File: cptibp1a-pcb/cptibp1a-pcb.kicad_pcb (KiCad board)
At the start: 2 copper layers, 50.5 x 42 mm, 28 parts, among them J1 10118194-0001LF, J2 PAD+, J3 PAD-, Q1 2N7002, Q2 AO3413, U1 NCP360SNT, U2 APX809S-31SA, U3 BQ21040, U4 APX810S-44SA, U5 NCP380HSN05

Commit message: cleanup
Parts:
- added REF**: ENCLOSURE, george:ENCLOSURE, F.Cu at (0.00, 0.00)
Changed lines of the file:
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@@
     )
   )
+  (footprint "george:ENCLOSURE" (layer "F.Cu")
+    (at 0 0)
+    (attr board_only allow_missing_courtyard)
+    (fp_text reference "REF**" (at 0 -0.5 unlocked) (layer "F.SilkS") hide
+        (effects (font (size 1 1) (thickness 0.15)))
+    )
+    (fp_text value "ENCLOSURE" (at 0 -4 unlocked) (layer "F.Fab")
+        (effects (font (size 1 1) (thickness 0.15)))
+    )
+    (fp_text user "${REFERENCE}" (at 0 4 unlocked) (layer "F.Fab")
+        (effects (font (size 1 1) (thickness 0.15)))
+    )
+    (fp_line (start -3 0) (end 3 0)
+      (stroke (width 0.12) (type default)) (layer "Dwgs.User"))
+    (fp_line (start 0 -3) (end 0 3)
+      (stroke (width 0.12) (type default)) (layer "Dwgs.User"))
+    (fp_circle (center 0 0) (end 0 -2)
+      (stroke (width 0.12) (type default)) (fill none) (layer "Dwgs.User"))
+  )
   (footprint "Capacitor_SMD:C_0805_2012Metric" (layer "F.Cu")
     (at 0.5 35.5 -90)
@@
   (gr_rect (start -12.6 27) (end -10 28.6)
     (stroke (width 0.15) (type default)) (fill none) (layer "F.SilkS"))
-  (gr_rect (start -0.2 25.5) (end 1.5 22.9)
+  (gr_rect (start -0.2 22.9) (end 1.5 25.5)
     (stroke (width 0.15) (type default)) (fill none) (layer "F.SilkS"))
   (gr_line (start -24.2 21.2) (end -23.8 20.8)
@@
   (gr_rect (start -9.7 18.6) (end -6.8 21.6)
     (stroke (width 0.15) (type default)) (fill none) (layer "F.SilkS"))
-  (gr_rect (start 5.65 27.65) (end 2.35 24.75)
+  (gr_rect (start 2.35 24.75) (end 5.65 27.65)
     (stroke (width 0.15) (type default)) (fill none) (layer "F.SilkS"))
-  (gr_rect (start 0.85 22.6) (end 6.45 19.4)
+  (gr_rect (start 0.85 19.4) (end 6.45 22.6)
     (stroke (width 0.15) (type default)) (fill none) (layer "F.SilkS"))
   (gr_rect (start -24.3 18.6) (end -21.7 20.3)

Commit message: rev1
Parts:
- added C3: 4u7, Capacitor_SMD:C_0805_2012Metric, F.Cu at (1.50, 39.1)
- added R6: 10k, Resistor_SMD:R_0805_2012Metric, F.Cu at (5.80, 35.5)
- added U6: NCP380HSN05, george:SOT-23-5_TI_DBV5, F.Cu at (4.70, 39.0)
- U5: value NCP380HSN05 -> MAX40203AUK
- moved U5 1.95 mm to (2.70, 35.5), turned to 0 degrees
- moved C2 1.76 mm to (-9.30, 39.1)
- moved U4 1.20 mm to (-5.59, 39.0)
- moved Q2 1.20 mm to (-1.50, 39.0)
- moved U2 1.09 mm to (-9.40, 31.4), turned to 180 degrees
- moved C4 0.95 mm to (-0.45, 35.5)
- moved R4 0.78 mm to (-11.5, 39.1), turned to 90 degrees
- moved R5 0.75 mm to (-7.95, 34.9)
- moved BT1 0.68 mm to (-4.20, 33.7)
- moved C6 0.25 mm to (11.4, 35.0)
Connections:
- C6 pad 1: /VOUT -> /VOUTF
- C7 pad 1: /VOUT -> /VOUTF
- D3 pad 1: /VOUT -> /VOUTF
- J2 pad 1: /VOUT -> /VOUTF
- U4 pad 3: /VOUT -> /VOUTF
- U5 pad 1: /VOUT -> /B+
- U5 pad 3: unconnected-(U5-~{OC}-Pad3) -> /EN
- U5 pad 4: /EN -> unconnected-(U5-NC-Pad4)
- U5 pad 5: /B+ -> /VOUT
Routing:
- net /VOUTF: track 0.00 -> 55.6 mm, vias 0 -> 3
- net /VOUT: track 47.7 -> 12.0 mm, vias 1 -> 0
- net /GND: track 28.5 -> 37.3 mm, vias 22 -> 23
- net /VCC: track 25.9 -> 23.4 mm
- net Net-(U6-~{OC}): track 0.00 -> 1.72 mm
- net /B+: track 17.4 -> 16.2 mm

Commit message: Rev1 update (minor)
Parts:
- moved J3 0.50 mm to (0.00, 12.5)
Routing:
- net /GND: track 37.3 -> 38.8 mm

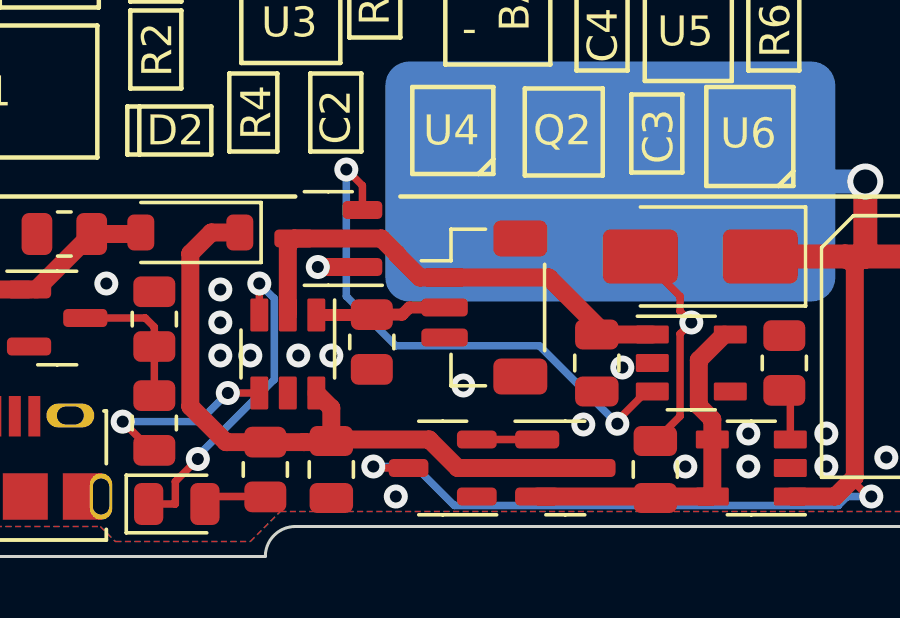
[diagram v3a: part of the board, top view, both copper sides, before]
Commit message: Move power connector (battery clash reduce)
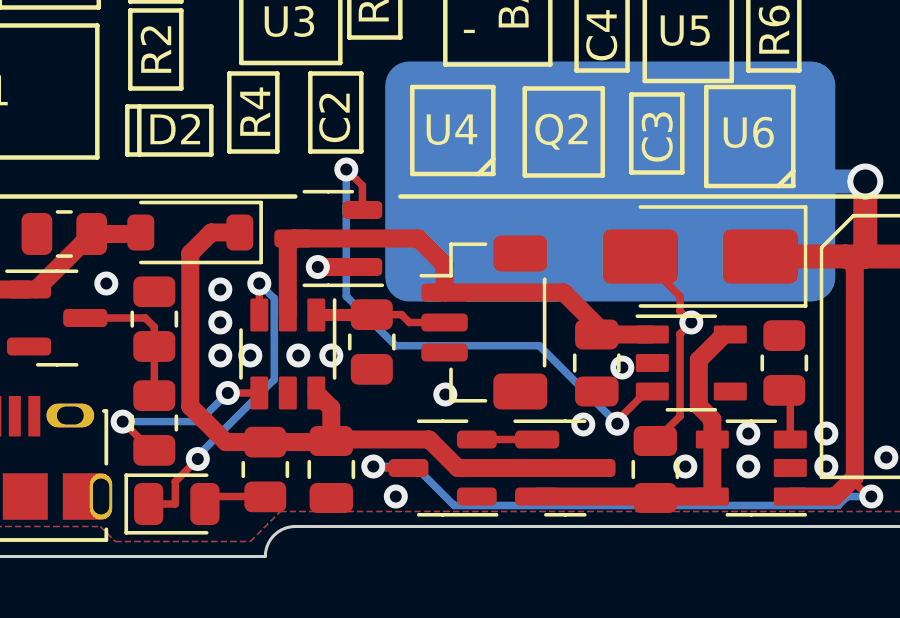
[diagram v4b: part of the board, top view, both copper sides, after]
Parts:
- moved BT1 0.50 mm to (-4.20, 34.2)
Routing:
- net /B+: track 16.2 -> 16.7 mm
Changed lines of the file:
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@@
       (sketchpadsonfab false)
       (subtractmaskfromsilk false)
-      (outputformat 4)
+      (outputformat 1)
       (mirror false)
       (drillshape 0)
@@
   )
   (footprint "Connector_JST:JST_SH_BM03B-SRSS-TB_1x03-1MP_P1.00mm_Vertical" (layer "F.Cu")
-    (at -4.2 33.7 -90)
+    (at -4.2 34.2 -90)
     (descr "JST SH series connector, BM03B-SRSS-TB (http://www.jst-mfg.com/product/pdf/eng/eSH.pdf), generated with kicad-footprint-generator")
     (tags "connector JST SH side entry")
@@
     (style (thickness 0.15) (arrow_length 1.27) (text_position_mode 0) (extension_height 0.58642) (extension_offset 0.5) keep_text_aligned)
   )
-  (segment (start -7.626606 31.4) (end -10.5375 31.4) (width 0.6) (layer "F.Cu") (net 1))
-  (segment (start -7.1 31.926606) (end -7.626606 31.4) (width 0.6) (layer "F.Cu") (net 1))
-  (segment (start -0.15 34.6) (end -2.05 32.7) (width 0.6) (layer "F.Cu") (net 1))
+  (segment (start -10.5375 31.4) (end -6.4 31.4) (width 0.6) (layer "F.Cu") (net 1))
+  (segment (start -5.525 33.2) (end -1.55 33.2) (width 0.6) (layer "F.Cu") (net 1))
   (segment (start 1.4 34.6) (end -0.45 34.6) (width 0.6) (layer "F.Cu") (net 1))
+  (segment (start -6.4 31.4) (end -5.525 32.275) (width 0.6) (layer "F.Cu") (net 1))
   (segment (start -10.75 31.6125) (end -10.5375 31.4) (width 0.6) (layer "F.Cu") (net 1))
-  (segment (start -7.1 31.95) (end -7.1 31.926606) (width 0.6) (layer "F.Cu") (net 1))
-  (segment (start -6.35 32.7) (end -7.1 31.95) (width 0.6) (layer "F.Cu") (net 1))
-  (segment (start -2.05 32.7) (end -6.35 32.7) (width 0.6) (layer "F.Cu") (net 1))
+  (segment (start -0.15 34.6) (end -1.55 33.2) (width 0.6) (layer "F.Cu") (net 1))
   (segment (start -10.75 33.95) (end -10.75 31.6125) (width 0.6) (layer "F.Cu") (net 1))
-  (segment (start -5.525 33.7) (end -6.7 33.7) (width 0.4) (layer "F.Cu") (net 2))
+  (segment (start -5.525 32.275) (end -5.525 33.2) (width 0.6) (layer "F.Cu") (net 1))
   (segment (start -9.8 33.95) (end -7.9625 33.95) (width 0.4) (layer "F.Cu") (net 2))
-  (segment (start -6.7 33.7) (end -6.9375 33.9375) (width 0.4) (layer "F.Cu") (net 2))
-  (segment (start -6.9375 33.9375) (end -7.95 33.9375) (width 0.4) (layer "F.Cu") (net 2))
+  (segment (start -6.7 34.2) (end -5.525 34.2) (width 0.25) (layer "F.Cu") (net 2))
+  (segment (start -7.95 33.9375) (end -6.9625 33.9375) (width 0.25) (layer "F.Cu") (net 2))
+  (segment (start -6.9625 33.9375) (end -6.7 34.2) (width 0.25) (layer "F.Cu") (net 2))
   (segment (start 2.325 37.325) (end 2.325 34.575) (width 0.25) (layer "F.Cu") (net 3))
   (segment (start 2.325 34.575) (end 2.7 34.2) (width 0.25) (layer "F.Cu") (net 3))
@@
   (via (at 4.6 37.9) (size 0.8) (drill 0.4) (layers "F.Cu" "B.Cu") (free) (net 3))
   (via (at 0.4 35.7) (size 0.8) (drill 0.4) (layers "F.Cu" "B.Cu") (free) (net 3))
-  (via (at -4.9 36.3) (size 0.8) (drill 0.4) (layers "F.Cu" "B.Cu") (free) (net 3))
+  (via (at -5.5 36.6) (size 0.8) (drill 0.4) (layers "F.Cu" "B.Cu") (free) (net 3))
   (via (at 13.8 38.7) (size 0.8) (drill 0.4) (layers "F.Cu" "B.Cu") (free) (net 3))
   (via (at -7.15 40) (size 0.8) (drill 0.4) (layers "F.Cu" "B.Cu") (free) (net 3))
